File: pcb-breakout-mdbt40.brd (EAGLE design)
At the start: 56.4 x 23.9 mm, 3 parts

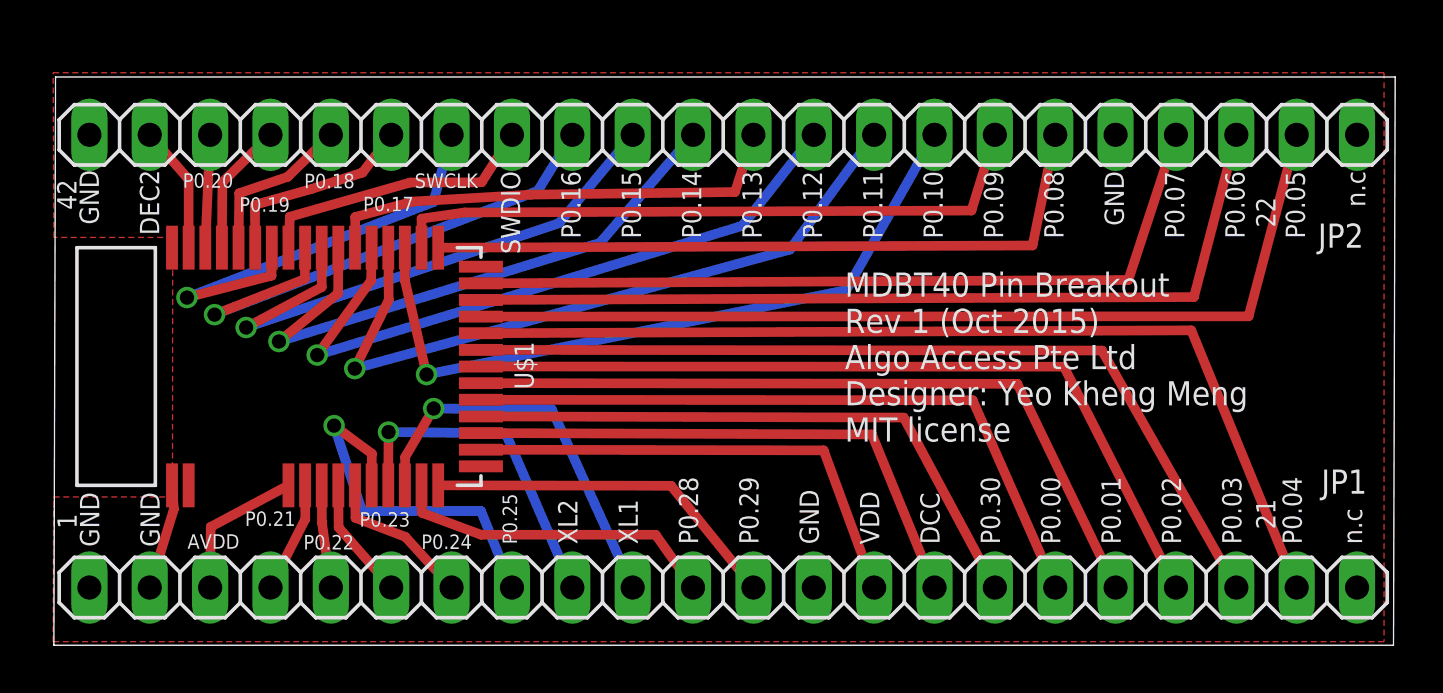
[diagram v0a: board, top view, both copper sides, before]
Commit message: prevent via short circuit
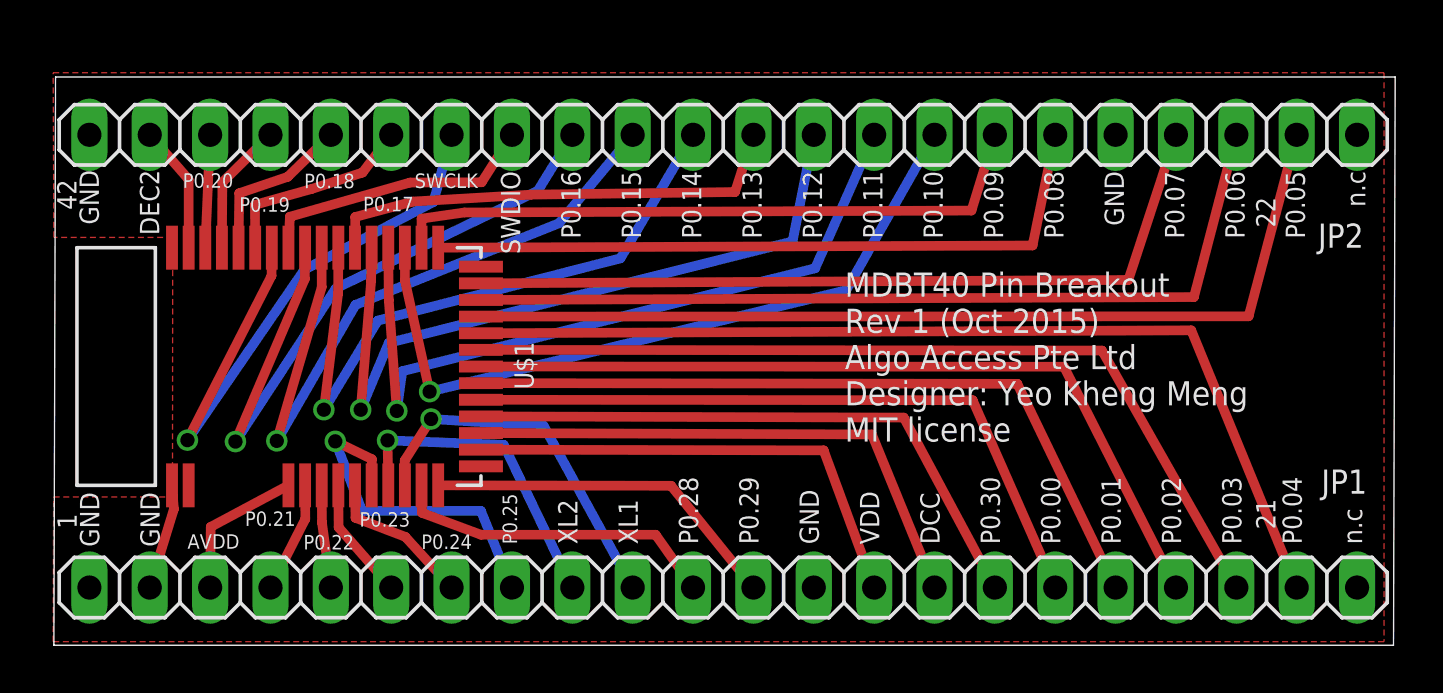
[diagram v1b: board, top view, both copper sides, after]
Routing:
- net N$28: track 18.9 -> 26.7 mm
- net N$30: track 22.7 -> 28.7 mm
- net N$31: track 24.0 -> 29.1 mm
- net N$34: track 28.8 -> 32.0 mm
- net N$32: track 25.3 -> 27.8 mm
- net N$35: track 30.4 -> 32.6 mm
- net N$10: track 16.8 -> 15.6 mm
- net N$8: track 15.6 -> 14.4 mm
- net N$9: track 14.2 -> 13.4 mm
- net N$36: track 31.0 -> 31.7 mm
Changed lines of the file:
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@@
 <contactref element="U$1" pad="8"/>
 <contactref element="JP1" pad="8"/>
-<wire x1="13.4" y1="6.078" x2="13.41" y2="7.41" width="0.4064" layer="1"/>
-<wire x1="13.41" y1="7.41" x2="11.82" y2="8.59" width="0.4064" layer="1"/>
-<via x="11.82" y="8.59" extent="1-16" drill="0.6" shape="square"/>
-<wire x1="11.82" y1="8.59" x2="13" y2="5" width="0.4064" layer="16"/>
+<wire x1="13.4" y1="6.078" x2="13.41" y2="7.18" width="0.4064" layer="1"/>
+<wire x1="13.41" y1="7.18" x2="11.87" y2="7.93" width="0.4064" layer="1"/>
+<via x="11.87" y="7.93" extent="1-16" drill="0.6" shape="square"/>
+<wire x1="11.87" y1="7.93" x2="13" y2="5" width="0.4064" layer="16"/>
 <wire x1="13" y1="5" x2="18" y2="5" width="0.4064" layer="16"/>
 <wire x1="18" y1="5" x2="19.304" y2="1.778" width="0.4064" layer="16"/>
@@
 <contactref element="U$1" pad="9"/>
 <contactref element="JP1" pad="9"/>
-<wire x1="14.1" y1="6.078" x2="14.11" y2="8.32" width="0.4064" layer="1"/>
-<via x="14.11" y="8.32" extent="1-16" drill="0.6" shape="square"/>
-<wire x1="14.11" y1="8.32" x2="19.04" y2="8.27" width="0.4064" layer="16"/>
-<wire x1="19.04" y1="8.27" x2="21.844" y2="1.778" width="0.4064" layer="16"/>
+<wire x1="14.1" y1="6.078" x2="14.07" y2="7.97" width="0.4064" layer="1"/>
+<via x="14.07" y="7.97" extent="1-16" drill="0.6" shape="square"/>
+<wire x1="14.07" y1="7.97" x2="18.96" y2="7.78" width="0.4064" layer="16"/>
+<wire x1="18.96" y1="7.78" x2="21.844" y2="1.778" width="0.4064" layer="16"/>
 </signal>
 <signal name="N$10">
 <contactref element="U$1" pad="10"/>
 <contactref element="JP1" pad="10"/>
-<via x="16.01" y="9.31" extent="1-16" drill="0.6" shape="square"/>
-<wire x1="16.01" y1="9.31" x2="20.98" y2="9.28" width="0.4064" layer="16"/>
-<wire x1="20.98" y1="9.28" x2="24.384" y2="1.778" width="0.4064" layer="16"/>
-<wire x1="14.8" y1="6.078" x2="14.81" y2="7.27" width="0.4064" layer="1"/>
-<wire x1="14.81" y1="7.27" x2="16.01" y2="9.31" width="0.4064" layer="1"/>
+<via x="15.9" y="8.87" extent="1-16" drill="0.6" shape="square"/>
+<wire x1="15.9" y1="8.87" x2="20.64" y2="8.58" width="0.4064" layer="16"/>
+<wire x1="20.64" y1="8.58" x2="24.384" y2="1.778" width="0.4064" layer="16"/>
+<wire x1="14.8" y1="6.078" x2="14.79" y2="7.12" width="0.4064" layer="1"/>
+<wire x1="14.79" y1="7.12" x2="15.9" y2="8.87" width="0.4064" layer="1"/>
 </signal>
 <signal name="N$11">
@@
 <contactref element="U$1" pad="36"/>
 <contactref element="JP2" pad="7"/>
-<via x="5.63" y="13.98" extent="1-16" drill="0.6" shape="square"/>
-<wire x1="5.63" y1="13.98" x2="16" y2="18" width="0.4064" layer="16"/>
+<via x="5.65" y="7.98" extent="1-16" drill="0.6" shape="square"/>
 <wire x1="16" y1="18" x2="16.764" y2="20.828" width="0.4064" layer="16"/>
 <wire x1="9.2" y1="16.078" x2="9.19" y2="14.9" width="0.4064" layer="1"/>
-<wire x1="9.19" y1="14.9" x2="5.63" y2="13.98" width="0.4064" layer="1"/>
+<wire x1="9.19" y1="14.9" x2="5.65" y2="7.98" width="0.4064" layer="1"/>
+<wire x1="16" y1="18" x2="10.57" y2="15.15" width="0.4064" layer="16"/>
+<wire x1="10.57" y1="15.15" x2="5.65" y2="7.98" width="0.4064" layer="16"/>
 </signal>
 <signal name="N$29">
@@
 <contactref element="U$1" pad="34"/>
 <contactref element="JP2" pad="9"/>
-<via x="6.79" y="13.26" extent="1-16" drill="0.6" shape="square"/>
-<wire x1="6.79" y1="13.26" x2="20.39" y2="18.47" width="0.4064" layer="16"/>
+<via x="7.67" y="7.92" extent="1-16" drill="0.6" shape="square"/>
 <wire x1="20.39" y1="18.47" x2="21.844" y2="20.828" width="0.4064" layer="16"/>
 <wire x1="10.6" y1="16.078" x2="10.59" y2="14.76" width="0.4064" layer="1"/>
-<wire x1="10.59" y1="14.76" x2="6.79" y2="13.26" width="0.4064" layer="1"/>
+<wire x1="10.59" y1="14.76" x2="7.67" y2="7.92" width="0.4064" layer="1"/>
+<wire x1="20.39" y1="18.47" x2="11.89" y2="14.36" width="0.4064" layer="16"/>
+<wire x1="11.89" y1="14.36" x2="7.67" y2="7.92" width="0.4064" layer="16"/>
 </signal>
 <signal name="N$31">
@@
 <contactref element="JP2" pad="10"/>
 <wire x1="11.3" y1="16.078" x2="11.3" y2="14.42" width="0.4064" layer="1"/>
-<wire x1="11.3" y1="14.42" x2="8.12" y2="12.72" width="0.4064" layer="1"/>
-<via x="8.12" y="12.72" extent="1-16" drill="0.6" shape="square"/>
-<wire x1="8.12" y1="12.72" x2="21.29" y2="17.11" width="0.4064" layer="16"/>
+<wire x1="11.3" y1="14.42" x2="9.41" y2="7.95" width="0.4064" layer="1"/>
+<via x="9.41" y="7.95" extent="1-16" drill="0.6" shape="square"/>
 <wire x1="21.29" y1="17.11" x2="24.384" y2="20.828" width="0.4064" layer="16"/>
+<wire x1="21.29" y1="17.11" x2="12.72" y2="13.67" width="0.4064" layer="16"/>
+<wire x1="12.72" y1="13.67" x2="9.41" y2="7.95" width="0.4064" layer="16"/>
 </signal>
 <signal name="N$32">
 <contactref element="U$1" pad="32"/>
 <contactref element="JP2" pad="11"/>
-<via x="9.5" y="12.13" extent="1-16" drill="0.6" shape="square"/>
-<wire x1="9.5" y1="12.13" x2="23.01" y2="16.28" width="0.4064" layer="16"/>
-<wire x1="23.01" y1="16.28" x2="26.924" y2="20.828" width="0.4064" layer="16"/>
+<via x="11.39" y="9.26" extent="1-16" drill="0.6" shape="square"/>
+<wire x1="23.87" y1="15.63" x2="26.924" y2="20.828" width="0.4064" layer="16"/>
 <wire x1="12" y1="16.078" x2="11.99" y2="14.16" width="0.4064" layer="1"/>
-<wire x1="11.99" y1="14.16" x2="9.5" y2="12.13" width="0.4064" layer="1"/>
+<wire x1="11.99" y1="14.16" x2="11.39" y2="9.26" width="0.4064" layer="1"/>
+<wire x1="23.87" y1="15.63" x2="13.66" y2="13.01" width="0.4064" layer="16"/>
+<wire x1="13.66" y1="13.01" x2="11.39" y2="9.26" width="0.4064" layer="16"/>
 </signal>
 <signal name="N$33">
@@
 <contactref element="JP2" pad="13"/>
 <wire x1="13.4" y1="16.078" x2="13.38" y2="14.7" width="0.4064" layer="1"/>
-<wire x1="13.38" y1="14.7" x2="11.11" y2="11.56" width="0.4064" layer="1"/>
-<via x="11.11" y="11.56" extent="1-16" drill="0.6" shape="square"/>
-<wire x1="11.11" y1="11.56" x2="29" y2="17" width="0.4064" layer="16"/>
-<wire x1="29" y1="17" x2="32.004" y2="20.828" width="0.4064" layer="16"/>
+<wire x1="13.38" y1="14.7" x2="12.94" y2="9.26" width="0.4064" layer="1"/>
+<via x="12.94" y="9.26" extent="1-16" drill="0.6" shape="square"/>
+<wire x1="31.11" y1="16.34" x2="32.004" y2="20.828" width="0.4064" layer="16"/>
+<wire x1="31.11" y1="16.34" x2="14.12" y2="12.07" width="0.4064" layer="16"/>
+<wire x1="14.12" y1="12.07" x2="12.94" y2="9.26" width="0.4064" layer="16"/>
 </signal>
 <signal name="N$35">
@@
 <contactref element="JP2" pad="14"/>
 <wire x1="14.1" y1="16.078" x2="14.12" y2="13.88" width="0.4064" layer="1"/>
-<wire x1="14.12" y1="13.88" x2="12.69" y2="10.99" width="0.4064" layer="1"/>
-<via x="12.69" y="10.99" extent="1-16" drill="0.6" shape="square"/>
-<wire x1="12.69" y1="10.99" x2="31" y2="16" width="0.4064" layer="16"/>
-<wire x1="31" y1="16" x2="34.544" y2="20.828" width="0.4064" layer="16"/>
+<wire x1="14.12" y1="13.88" x2="14.46" y2="9.21" width="0.4064" layer="1"/>
+<via x="14.46" y="9.21" extent="1-16" drill="0.6" shape="square"/>
+<wire x1="32.06" y1="15.21" x2="34.544" y2="20.828" width="0.4064" layer="16"/>
+<wire x1="14.46" y1="9.21" x2="14.69" y2="10.88" width="0.4064" layer="16"/>
+<wire x1="14.69" y1="10.88" x2="32.06" y2="15.21" width="0.4064" layer="16"/>
 </signal>
 <signal name="N$36">
 <contactref element="U$1" pad="28"/>
 <contactref element="JP2" pad="15"/>
-<via x="15.71" y="10.74" extent="1-16" drill="0.6" shape="square"/>
-<wire x1="15.71" y1="10.74" x2="33.37" y2="14.29" width="0.4064" layer="16"/>
+<via x="15.84" y="10.02" extent="1-16" drill="0.6" shape="square"/>
+<wire x1="15.84" y1="10.02" x2="33.37" y2="14.29" width="0.4064" layer="16"/>
 <wire x1="33.37" y1="14.29" x2="37.084" y2="20.828" width="0.4064" layer="16"/>
 <wire x1="14.8" y1="16.078" x2="14.8" y2="14.7" width="0.4064" layer="1"/>
-<wire x1="14.8" y1="14.7" x2="15.71" y2="10.74" width="0.4064" layer="1"/>
+<wire x1="14.8" y1="14.7" x2="15.84" y2="10.02" width="0.4064" layer="1"/>
 </signal>
 <signal name="N$37">

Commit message: enlarged board width and shifting JP2
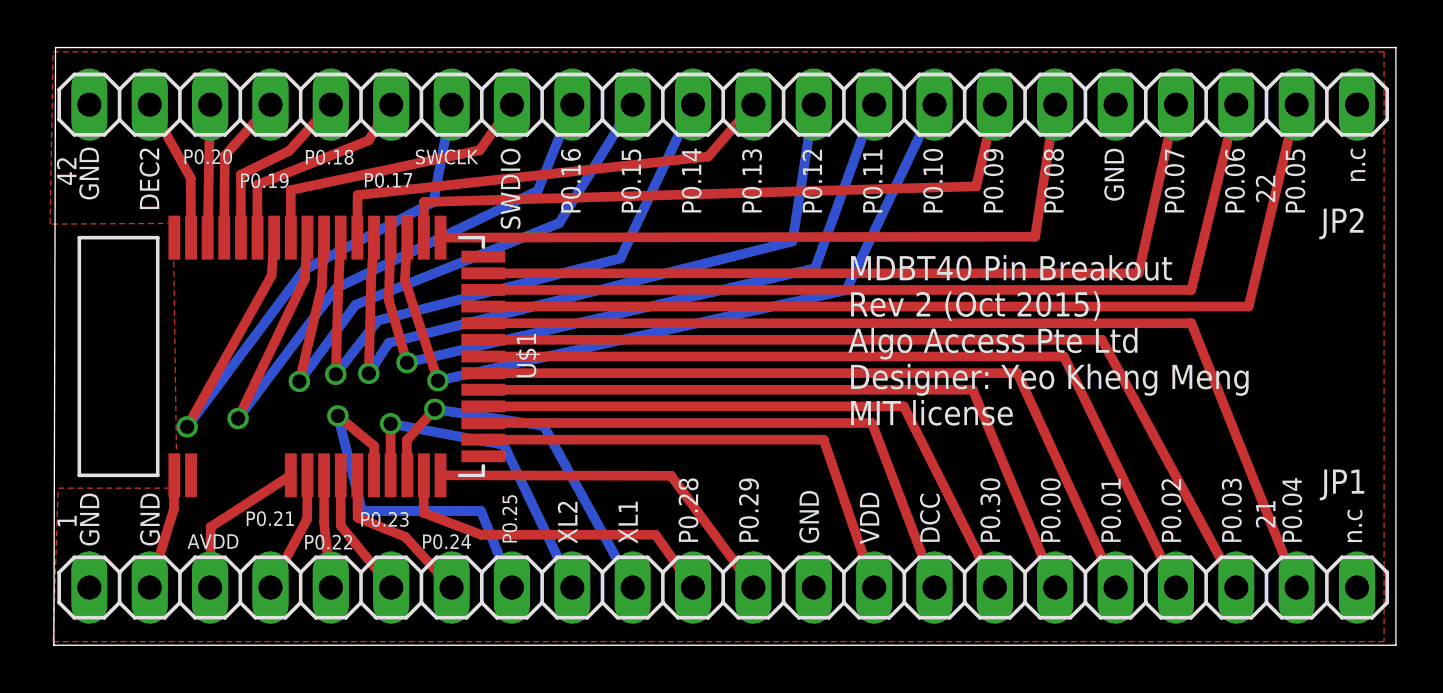
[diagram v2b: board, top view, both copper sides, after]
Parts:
- moved JP2 1.27 mm to (28.2, 22.1)
- moved U$1 0.43 mm to (9.10, 11.5)
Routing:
- net N$31: track 29.1 -> 25.3 mm
- net N$35: track 32.6 -> 30.3 mm
- net N$32: track 27.8 -> 26.3 mm
- net N$8: track 14.4 -> 15.8 mm
- net N$34: track 32.0 -> 30.6 mm
- net N$40: track 33.7 -> 34.8 mm
- net N$38: track 29.8 -> 30.6 mm
- net N$24: track 4.75 -> 5.60 mm
- net N$41: track 37.1 -> 37.8 mm
- net N$36: track 31.7 -> 32.5 mm
- net N$25: track 5.60 -> 6.33 mm
- net N$42: track 40.2 -> 40.9 mm
- net N$28: track 26.7 -> 27.4 mm
- net N$23: track 5.36 -> 6.05 mm
- net N$37: track 27.7 -> 28.3 mm
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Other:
- board size 56.4 x 23.9 mm -> 56.5 x 25.1 mm
- board text added: "MDBT40 Pin Breakout Rev 2 (Oct 2015) Algo Access Pte Ltd Designer: Yeo Kheng Meng MIT license"
- board text removed: "MDBT40 Pin Breakout Rev 1 (Oct 2015) Algo Access Pte Ltd Designer: Yeo Kheng Meng MIT license"
